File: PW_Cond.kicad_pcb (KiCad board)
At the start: 2 copper layers, 25 parts, among them J1 Conn_01x02_Female, J2 Conn_01x04_Female, J3 Conn_01x02_Female, Q1 BC847, U1 MCP602, U2 MCP602

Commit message: psb is going well
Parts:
- moved R3 96.0 mm to (104.0, 111.0), turned to 270 degrees
- moved R5 92.4 mm to (109.0, 117.0), turned to 180 degrees
- moved R8 86.8 mm to (114.0, 117.0), turned to 180 degrees
- moved H4 86.5 mm to (100.0, 125.0)
- moved R1 86.4 mm to (105.1, 103.6), turned to 270 degrees
- moved Q1 85.8 mm to (108.0, 122.0), turned to 90 degrees
- moved J1 81.0 mm to (111.2, 100.0), turned to 90 degrees
- moved R11 78.6 mm to (115.7, 91.9)
- moved H1 77.6 mm to (100.0, 100.0)
- moved R4 75.6 mm to (110.0, 104.0), turned to 180 degrees
- moved R7 75.2 mm to (116.0, 104.0), turned to 180 degrees
- moved R9 72.6 mm to (114.0, 114.0), turned to 180 degrees
- moved H3 69.3 mm to (130.0, 125.0)
- moved R10 67.8 mm to (123.0, 104.0), turned to 180 degrees
- moved C1 67.5 mm to (114.0, 110.0), turned to 90 degrees
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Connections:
- U2 pad 1: Net-(Q1-Pad1) -> /Meusure
- U2 pad 2: Net-(Q1-Pad2) -> Net-(R10-Pad2)
- U2 pad 3: Net-(D1-Pad1) -> Net-(R8-Pad1)
- U2 pad 5: Net-(R8-Pad1) -> Net-(D1-Pad1)
- U2 pad 6: Net-(R10-Pad2) -> Net-(Q1-Pad2)
- U2 pad 7: /Meusure -> Net-(Q1-Pad1)
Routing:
- added copper zone on F.Cu, net GND
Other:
- board outline added: 38 x 33 mm

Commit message: placement seems to be finished
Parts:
- moved R11 9.83 mm to (115.6, 101.7), turned to 180 degrees
- moved D2 8.43 mm to (121.0, 100.0)
- moved R1 6.04 mm to (104.4, 109.6)
- moved J3 6.00 mm to (130.0, 111.2)
- moved R6 5.91 mm to (122.0, 125.8)
- moved R5 5.13 mm to (108.0, 122.0)
- moved R8 5.12 mm to (115.0, 122.0)
- moved R3 5.06 mm to (104.4, 116.1)
- moved D1 5.04 mm to (122.0, 122.0)
- moved R9 4.33 mm to (115.0, 118.2)
- moved Q1 4.11 mm to (107.9, 126.1)
- moved R2 3.96 mm to (115.0, 125.8)
- moved J1 2.96 mm to (108.3, 100.0)
- moved C1 2.81 mm to (115.2, 112.5)
- moved C2 2.70 mm to (126.0, 112.5), turned to 90 degrees
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
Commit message: board v1 finished
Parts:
- H1, H2, H3, H4: footprint MountingHole:MountingHole_3.2mm_M3_Pad_Via -> MountingHole:MountingHole_2.2mm_M2_Pad_Via
- moved R9 13.6 mm to (115.2, 104.7), turned to 0 degrees
- moved R11 10.8 mm to (105.1, 99.6), turned to 0 degrees
- moved H3 8.54 mm to (122.0, 122.0)
- moved J3 8.14 mm to (122.0, 109.7)
- moved R6 8.08 mm to (116.5, 119.9), turned to 0 degrees
- moved H2 8.00 mm to (122.0, 100.0)
- moved C2 7.73 mm to (118.4, 111.2)
- moved R1 7.49 mm to (105.1, 102.1), turned to 180 degrees
- moved D1 7.19 mm to (116.5, 117.3)
- moved U2 7.14 mm to (114.0, 111.0)
- moved R8 6.28 mm to (110.8, 117.3)
- moved C1 5.85 mm to (109.5, 111.2)
- moved Q1 5.71 mm to (110.8, 121.2), turned to 180 degrees
- moved R7 5.54 mm to (110.2, 104.7)
- moved R5 5.52 mm to (105.1, 117.3)
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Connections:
- D2 pad 1: Net-(D2-Pad1) -> GND
- D2 pad 2: +15V -> Net-(D2-Pad2)
- R11 pad 1: Net-(D2-Pad1) -> +15V
- R11 pad 2: GND -> Net-(D2-Pad2)
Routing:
- net +15V: track 0.00 -> 56.7 mm, vias 0 -> 2
- net Net-(D1-Pad1): track 0.00 -> 27.1 mm
- net Net-(R3-Pad1): track 0.00 -> 18.2 mm, vias 0 -> 2
- net Net-(R10-Pad2): track 0.00 -> 16.3 mm
- net Net-(Q1-Pad2): track 0.00 -> 15.2 mm
- net /MAP: track 0.00 -> 14.4 mm
- net Net-(R8-Pad1): track 0.00 -> 14.2 mm
- net /Meusure: track 0.00 -> 11.3 mm
- net GND: track 0.00 -> 10.6 mm, vias 0 -> 7
- net Net-(D2-Pad2): track 0.00 -> 10.5 mm
- net Net-(Q1-Pad1): track 0.00 -> 9.95 mm
- net /PAP: track 0.00 -> 7.50 mm
- net Net-(R5-Pad1): track 0.00 -> 7.48 mm
- net Net-(R4-Pad1): track 0.00 -> 7.04 mm
- net Net-(R3-Pad2): track 0.00 -> 6.35 mm
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- added copper zone on B.Cu, net GND
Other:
- board size 38 x 33 mm -> 30 x 30 mm

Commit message: kicad logo + minor tweaks
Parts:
- added S1: KiCad-Logo2_6mm_SilkScreen, Symbol:KiCad-Logo2_6mm_SilkScreen, B.Cu at (111.0, 120.0)
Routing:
- net /Meusure: track 11.3 -> 12.9 mm
- net +15V: track 56.7 -> 58.3 mm
- net GND: vias 7 -> 25
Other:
- net class Masse added: clearance 0.2, trace_width 0.5, via_dia 1, via_drill 0.4
- board text added: "+"
- board text added: "-"

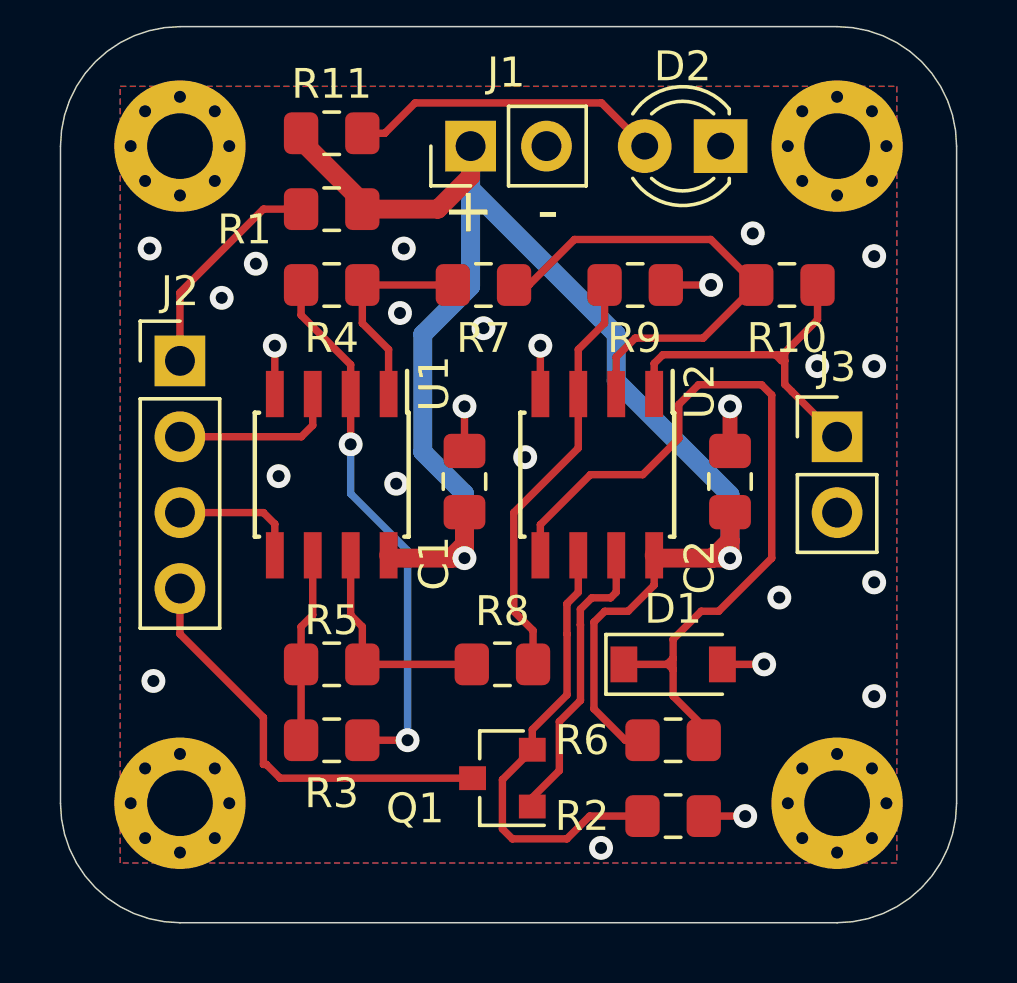
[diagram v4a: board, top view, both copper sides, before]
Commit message: tweaks on signals + vias
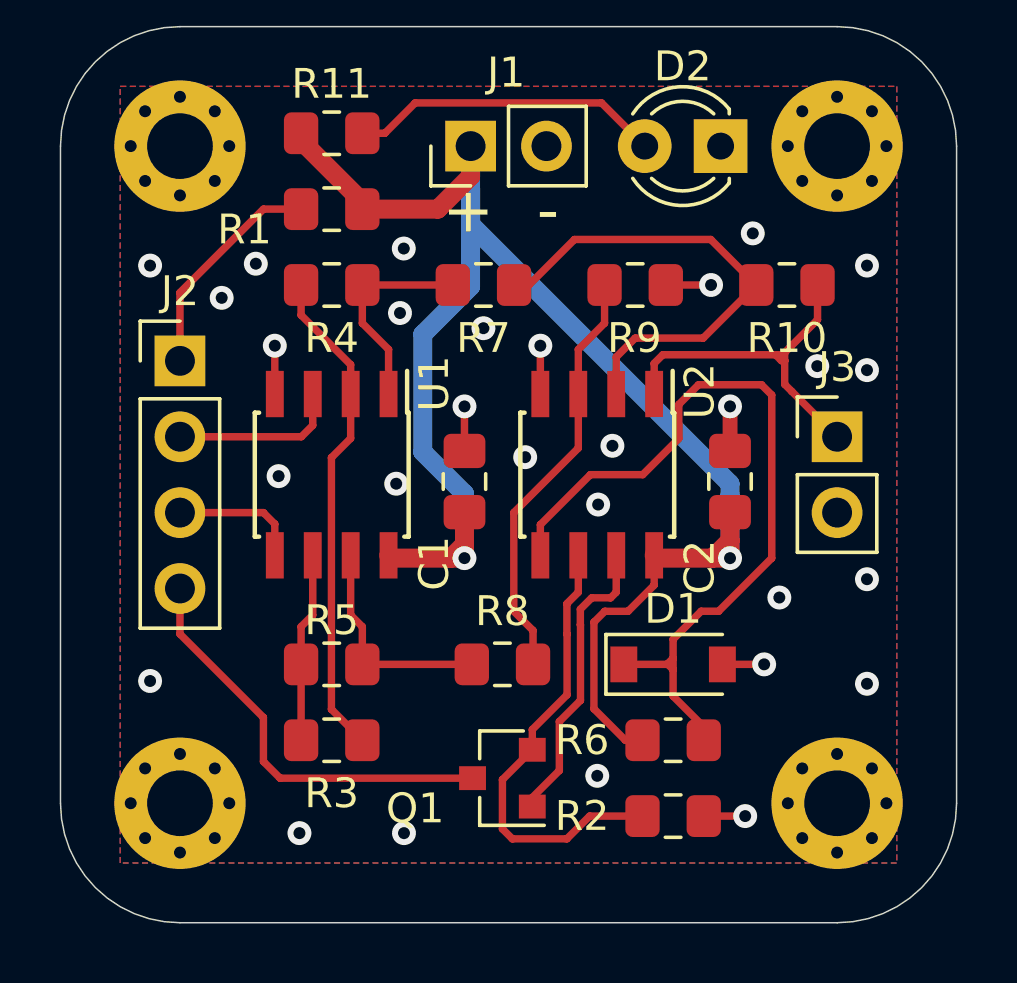
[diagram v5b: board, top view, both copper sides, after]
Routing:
- net Net-(R3-Pad1): track 18.2 -> 16.6 mm, vias 2 -> 0
- net GND: vias 25 -> 29

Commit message: Mod serigraphie
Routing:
- net GND: vias 29 -> 28
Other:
- board text added: "GND"
- board text added: "MAP"
- board text added: "NMP"
- board text added: "OUT"
- board text added: "PAP"
- board text added: "PMP"
